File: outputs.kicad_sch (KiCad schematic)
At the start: 2 parts, among them U2 TPS1HB08BQPWPRQ1

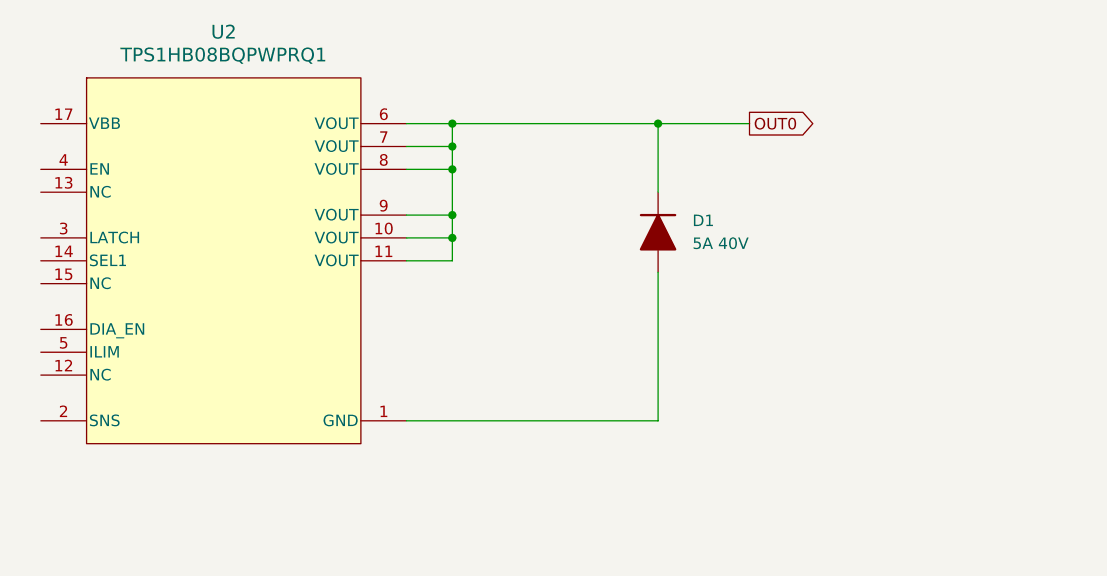
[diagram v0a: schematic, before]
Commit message: More sheets and switching to external FET HSS
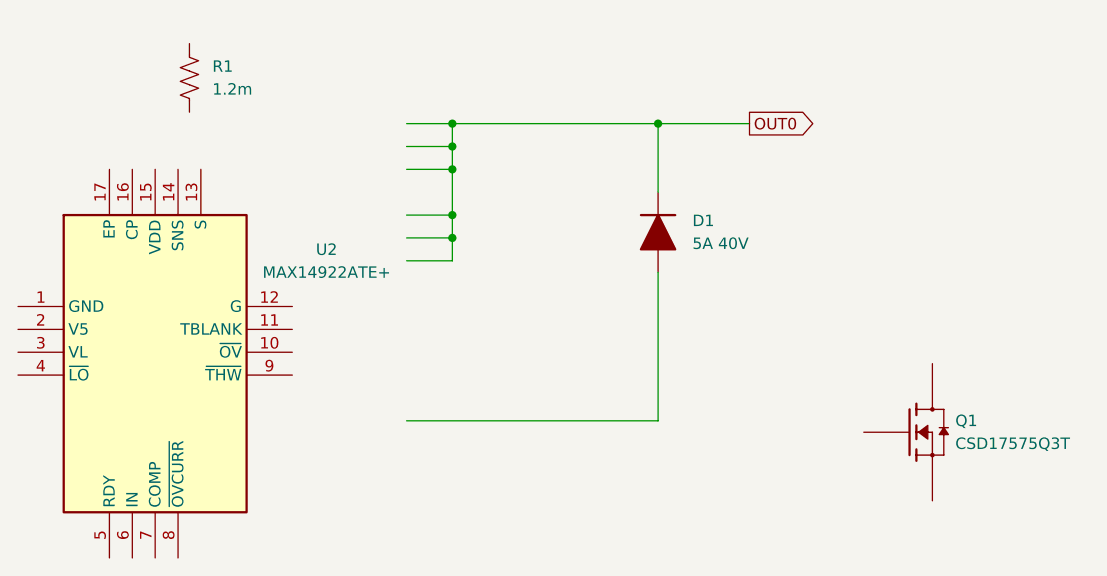
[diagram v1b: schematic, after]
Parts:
- removed U2: TPS1HB08BQPWPRQ1, Sullivan-Labs:PWP0016M-IPC_A, symbol Sullivan-Labs:IC TI High Side Switch 12V 6-70A
- added Q1: CSD17575Q3T, Sullivan-Labs:TRANS_CSD17308Q3, symbol Sullivan-Labs:NMOS 60A 30V
- added R1: 1.2m, Sullivan-Labs:R_2512_6332Metric_Pad1.40x3.35mm_HandSolder, symbol Sullivan-Labs:RES_1.2m_2512
- added U2: MAX14922ATE+, Sullivan-Labs:QFN50P300X300X80-17N, symbol Sullivan-Labs:IC High Side Switch Ex FET
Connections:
- new net: Q1.1 (S), Q1.2 (S), Q1.3 (S)
- new net: Q1.5 (D), Q1.6 (D), Q1.7 (D), Q1.8 (D), Q1.9 (D)
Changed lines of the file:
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@@
+	)
+	(symbol
+		(lib_id "Sullivan-Labs:RES_1.2m_2512")
+		(at 55.88 27.94 0)
+		(unit 1)
+		(exclude_from_sim no)
+		(in_bom yes)
+		(on_board yes)
+		(dnp no)
+		(fields_autoplaced yes)
+		(property "Reference" "R1"
+			(at 58.42 26.6699 0)
+			(effects
+				(font
+					(size 1.27 1.27)
+				)
+				(justify left)
+			)
+		)
+		(property "Value" "1.2m"
+			(at 58.42 29.2099 0)
+			(effects
+				(font
+					(size 1.27 1.27)
+				)
+				(justify left)
+			)
+		)
+		(property "Footprint" "Sullivan-Labs:R_2512_6332Metric_Pad1.40x3.35mm_HandSolder"
+			(at 56.896 28.194 90)
+			(effects
+				(font
+					(size 1.27 1.27)
+				)
+				(hide yes)
+			)
+		)
+		(property "Datasheet" "~"
+			(at 55.88 27.94 0)
+			(effects
+				(font
+					(size 1.27 1.27)
+				)
+				(hide yes)
+			)
+		)
+		(property "Description" "1.2mOhm 5W Shunt Resistor"
+			(at 55.88 27.94 0)
+			(effects
+				(font
+					(size 1.27 1.27)
+				)
+				(hide yes)
+			)
+		)
+		(property "Manufacturer" "VPG Foil Resistors"
+			(at 55.88 27.94 0)
+			(effects
+				(font
+					(size 1.27 1.27)
+				)
+				(hide yes)
+			)
+		)
+		(property "PN" "Y14830R00120F9R"
+			(at 55.88 27.94 0)
+			(effects
+				(font
+					(size 1.27 1.27)
+				)
+				(hide yes)
+			)
+		)
+		(pin "2"
+		)
+		(pin "1"
+		)
+		(instances
+			(project ""
+				(path "/d013d610-c58f-4b11-9d18-37fc135ac516/7b650159-18e3-4a88-b5a2-506e6fe9f3ef"
+					(reference "R1")
+					(unit 1)
+				)
+			)
+		)
+	)
+	(symbol
+		(lib_id "Sullivan-Labs:IC High Side Switch Ex FET")
+		(at 36.83 53.34 0)
+		(unit 1)
+		(exclude_from_sim no)
+		(in_bom yes)
+		(on_board yes)
+		(dnp no)
+		(fields_autoplaced yes)
+		(property "Reference" "U2"
+			(at 71.12 47.0214 0)
+			(effects
+				(font
+					(size 1.27 1.27)
+				)
+			)
+		)
+		(property "Value" "MAX14922ATE+"
+			(at 71.12 49.5614 0)
+			(effects
+				(font
+					(size 1.27 1.27)
+				)
+			)
+		)
+		(property "Footprint" "Sullivan-Labs:QFN50P300X300X80-17N"
+			(at 63.5 140.64 0)
+			(effects
+				(font
+					(size 1.27 1.27)
+				)
+				(justify left top)
+				(hide yes)
+			)
+		)
+		(property "Datasheet" "https://pdfserv.maximintegrated.com/en/ds/MAX14922.pdf"
+			(at 63.5 240.64 0)
+			(effects
+				(font
+					(size 1.27 1.27)
+				)
+				(justify left top)
+				(hide yes)
+			)
+		)
+		(property "Description" "Switching Controllers High-Side Switch Controller"
+			(at 36.83 53.34 0)
+			(effects
+				(font
+					(size 1.27 1.27)
+				)
+				(hide yes)
+			)
+		)
+		(property "Manufacturer" "Analog Devices"
+			(at 63.5 540.64 0)
+			(effects
+				(font
+					(size 1.27 1.27)
+				)
+				(justify left top)
+				(hide yes)
+			)
+		)
+		(property "PN" "MAX14922ATE+"
+			(at 63.5 640.64 0)
+			(effects
+				(font
+					(size 1.27 1.27)
+				)
+				(justify left top)
+				(hide yes)
+			)
+		)
+		(pin "10"
+		)
+		(pin "1"
+		)
+		(pin "17"
+		)
+		(pin "15"
+		)
+		(pin "14"
+		)
+		(pin "13"
+		)
+		(pin "9"
+		)
+		(pin "3"
+		)
+		(pin "2"
+		)
+		(pin "16"
+		)
+		(pin "5"
+		)
+		(pin "11"
+		)
+		(pin "6"
+		)
+		(pin "7"
+		)
+		(pin "8"
+		)
+		(pin "4"
+		)
+		(pin "12"
+		)
+		(instances
+			(project ""
+				(path "/d013d610-c58f-4b11-9d18-37fc135ac516/7b650159-18e3-4a88-b5a2-506e6fe9f3ef"
+					(reference "U2")
+					(unit 1)
+				)
+			)
+		)
 	)
 	(symbol
@@
 	)
 	(symbol
-		(lib_id "Sullivan-Labs:IC TI High Side Switch 12V 6-70A")
-		(at 39.37 33.02 0)
+		(lib_id "Sullivan-Labs:NMOS 60A 30V")
+		(at 135.89 67.31 0)
 		(unit 1)
 		(exclude_from_sim no)
@@
 		(dnp no)
 		(fields_autoplaced yes)
-		(property "Reference" "U2"
-			(at 59.69 22.86 0)
-			(effects
-				(font
-					(size 1.524 1.524)
-				)
-			)
-		)
-		(property "Value" "TPS1HB08BQPWPRQ1"
-			(at 59.69 25.4 0)
-			(effects
-				(font
-					(size 1.524 1.524)
-				)
-			)
-		)
-		(property "Footprint" "Sullivan-Labs:PWP0016M-IPC_A"
-			(at 39.37 33.02 0)
-			(effects
-				(font
-					(size 1.27 1.27)
-					(italic yes)
-				)
-				(hide yes)
-			)
-		)
-		(property "Datasheet" "TPS1HB08BQPWPRQ1"
-			(at 39.37 33.02 0)
-			(effects
-				(font
-					(size 1.27 1.27)
-					(italic yes)
-				)
-				(hide yes)
-			)
-		)
-		(property "Description" "Power Switch ICs - Power Distribution 40-V, 8-mohm, 1-ch automotive smart high-side switch with adjustable current limit 16-HTSSOP -40 to 125"
-			(at 39.37 33.02 0)
-			(effects
-				(font
-					(size 1.27 1.27)
-				)
-				(hide yes)
-			)
-		)
-		(property "Manufacturer" " Texas Instruments"
-			(at 39.37 33.02 0)
-			(effects
-				(font
-					(size 1.27 1.27)
-				)
-				(hide yes)
-			)
-		)
-		(property "PN" "TPS1HB08BQPWPRQ1"
-			(at 39.37 33.02 0)
-			(effects
-				(font
-					(size 1.27 1.27)
-				)
-				(hide yes)
-			)
-		)
-		(pin "10"
+		(property "Reference" "Q1"
+			(at 140.97 66.0399 0)
+			(effects
+				(font
+					(size 1.27 1.27)
+				)
+				(justify left)
+			)
+		)
+		(property "Value" "CSD17575Q3T"
+			(at 140.97 68.5799 0)
+			(effects
+				(font
+					(size 1.27 1.27)
+				)
+				(justify left)
+			)
+		)
+		(property "Footprint" "Sullivan-Labs:TRANS_CSD17308Q3"
+			(at 129.794 92.456 0)
+			(effects
+				(font
+					(size 1.27 1.27)
+				)
+				(justify bottom)
+				(hide yes)
+			)
+		)
+		(property "Datasheet" ""
+			(at 131.318 84.328 0)
+			(effects
+				(font
+					(size 1.27 1.27)
+				)
+				(hide yes)
+			)
+		)
+		(property "Description" "MOSFETs 30V,NCh NexFET Pwr MOSFET"
+			(at 130.556 90.932 0)
+			(effects
+				(font
+					(size 1.27 1.27)
+				)
+				(hide yes)
+			)
+		)
+		(property "Manufacturer" "Texas Instruments"
+			(at 131.318 84.328 0)
+			(effects
+				(font
+					(size 1.27 1.27)
+				)
+				(justify bottom)
+				(hide yes)
+			)
+		)
+		(property "PN" "CSD17575Q3T"
+			(at 131.318 84.328 0)
+			(effects
+				(font
+					(size 1.27 1.27)
+				)
+				(justify bottom)
+				(hide yes)
+			)
+		)
+		(pin "6"
 		)
 		(pin "1"
@@
 		(pin "7"
 		)
+		(pin "9"
+		)
+		(pin "5"
+		)
+		(pin "2"
+		)
+		(pin "4"
+		)
 		(pin "3"
 		)
-		(pin "9"
-		)
-		(pin "17"
-		)
-		(pin "5"
-		)
-		(pin "12"
-		)
-		(pin "2"
-		)
-		(pin "16"
-		)
-		(pin "4"
-		)
-		(pin "15"
-		)
-		(pin "13"
-		)
 		(pin "8"
-		)
-		(pin "6"
-		)
-		(pin "14"
-		)
-		(pin "11"
 		)
 		(instances
 			(project ""
 				(path "/d013d610-c58f-4b11-9d18-37fc135ac516/7b650159-18e3-4a88-b5a2-506e6fe9f3ef"
-					(reference "U2")
+					(reference "Q1")
 					(unit 1)
 				)

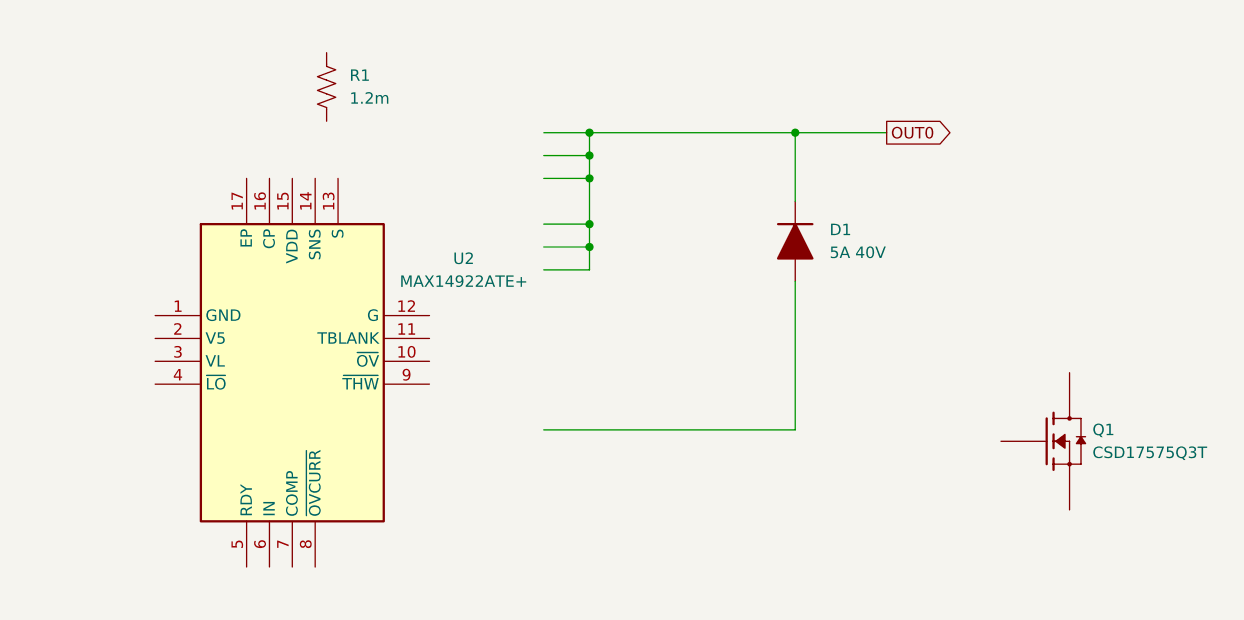
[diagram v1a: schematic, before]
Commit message: Added power domain stuff
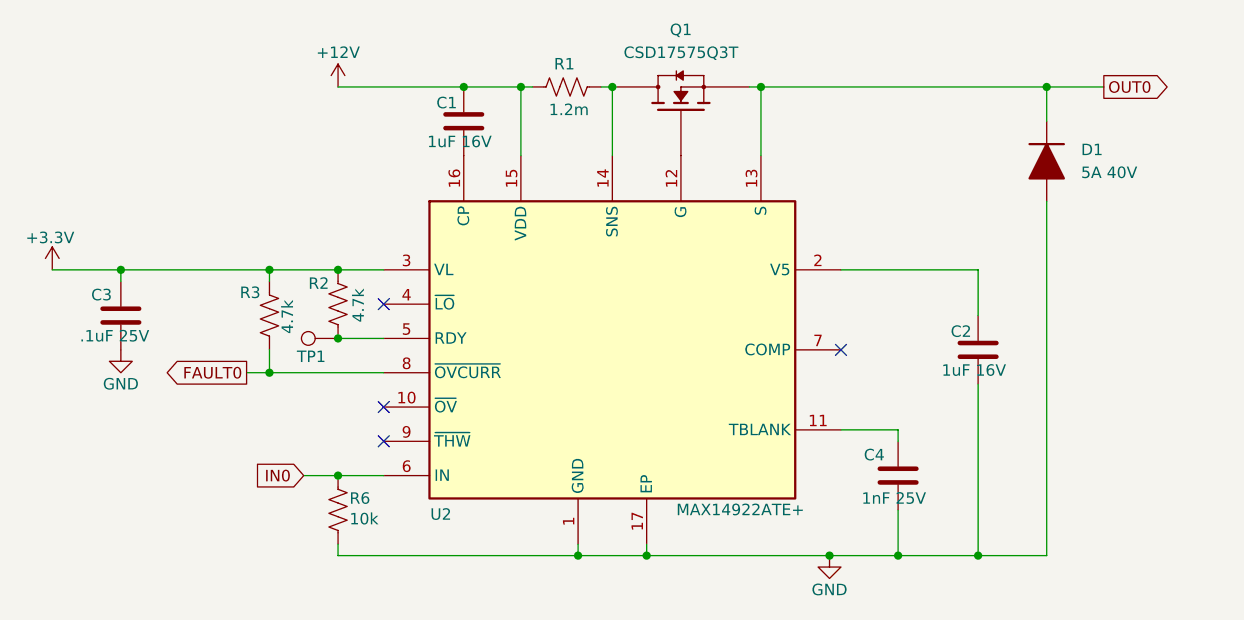
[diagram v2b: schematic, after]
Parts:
- added C1, C2: 1uF 16V, Sullivan-Labs:C_0402_1005Metric, symbol Sullivan-Labs:CAP_1uF_16V_0402
- added C3: .1uF 25V, Sullivan-Labs:C_0402_1005Metric, symbol Sullivan-Labs:CAP_.1uF_25V_0402
- added C4: 1nF 25V, Sullivan-Labs:C_0402_1005Metric, symbol Sullivan-Labs:CAP_1nF_25V_0402
- added R2, R3: 4.7k, Sullivan-Labs:R_0402_1005Metric, symbol Sullivan-Labs:RES_4.7k_0402
- added R6: 10k, Sullivan-Labs:R_0402_1005Metric, symbol Sullivan-Labs:RES_10k_0402
- added TP1: TestPoint, Sullivan-Labs:TestPoint_Pad_D1.0mm, symbol Sullivan-Labs:TP 1mm Circle
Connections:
- net OUT0: now also Q1.1 (S), Q1.2 (S), Q1.3 (S), U2.13 (S)
- net +12V: now reaches R1.1
- net +12V: now also U2.15 (VDD), C1.1
- net at R1.2: now also Q1.5 (D), Q1.6 (D), Q1.7 (D), Q1.8 (D), Q1.9 (D), U2.14 (SNS)
- net GND: now reaches U2.1 (GND)
- net GND: now also D1.2 (A), U2.17 (EP), C2.2, C3.2, C4.2, R6.2
- net at U2.11 (TBLANK): now also C4.1
- net at U2.12 (G): now also Q1.4 (G)
- net at U2.16 (CP): now also C1.2
- net at U2.2 (V5): now also C2.1
- net +3.3V: now reaches U2.3 (VL)
- net +3.3V: now also C3.1, R2.1, R3.1
- net at U2.5 (RDY): now also R2.2, TP1.1
- net IN0: now reaches U2.6 (IN)
- net IN0: now also R6.1
- net FAULT0: now reaches U2.8 (~{OVCURR})
- net FAULT0: now also R3.2
- no-connect marks 0 -> 4
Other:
- moved on the sheet: D1, Q1, R1, U2

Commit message: Small changes to schematic
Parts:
- added R43: 4.7k, Sullivan-Labs:R_0402_1005Metric, symbol Sullivan-Labs:RES_4.7k_0402
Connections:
- net +3.3V: now also R43.1
- net OVERHEAT: now reaches U2.9 (~{THW})
- net OVERHEAT: now also R43.2
- no-connect marks 4 -> 3
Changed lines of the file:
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@@
-	)
-	(no_connect
-		(at 62.23 67.31)
 	)
 	(no_connect
@@
 	(wire
 		(pts
+			(xy 46.99 67.31) (xy 62.23 67.31)
+		)
+		(stroke
+			(width 0)
+			(type default)
+		)
+	)
+	(wire
+		(pts
 			(xy 135.89 27.94) (xy 135.89 31.75)
 		)
@@
 	(wire
 		(pts
+			(xy 243.84 120.65) (xy 246.38 120.65)
+		)
+		(stroke
+			(width 0)
+			(type default)
+		)
+	)
+	(wire
+		(pts
 			(xy 77.47 27.94) (xy 78.74 27.94)
 		)
@@
 		(pts
 			(xy 49.53 49.53) (xy 49.53 48.26)
+		)
+		(stroke
+			(width 0)
+			(type default)
+		)
+	)
+	(wire
+		(pts
+			(xy 246.38 119.38) (xy 246.38 120.65)
 		)
 		(stroke
@@
 		(property "Intersheetrefs" "${INTERSHEET_REFS}"
 			(at 47.21 71.12 0)
+			(effects
+				(font
+					(size 1.27 1.27)
+				)
+				(justify right)
+				(hide yes)
+			)
+		)
+	)
+	(global_label "OVERHEAT"
+		(shape output)
+		(at 46.99 67.31 180)
+		(fields_autoplaced yes)
+		(effects
+			(font
+				(size 1.27 1.27)
+			)
+			(justify right)
+		)
+		(property "Intersheetrefs" "${INTERSHEET_REFS}"
+			(at 34.631 67.31 0)
+			(effects
+				(font
+					(size 1.27 1.27)
+				)
+				(justify right)
+				(hide yes)
+			)
+		)
+	)
+	(global_label "OVERHEAT"
+		(shape output)
+		(at 243.84 120.65 180)
+		(fields_autoplaced yes)
+		(effects
+			(font
+				(size 1.27 1.27)
+			)
+			(justify right)
+		)
+		(property "Intersheetrefs" "${INTERSHEET_REFS}"
+			(at 231.481 120.65 0)
 			(effects
 				(font
@@
 	)
 	(symbol
+		(lib_id "Sullivan-Labs:RES_4.7k_0402")
+		(at 246.38 115.57 0)
+		(unit 1)
+		(exclude_from_sim no)
+		(in_bom yes)
+		(on_board yes)
+		(dnp no)
+		(property "Reference" "R43"
+			(at 244.094 117.348 90)
+			(effects
+				(font
+					(size 1.27 1.27)
+				)
+				(justify left)
+			)
+		)
+		(property "Value" "4.7k"
+			(at 248.412 117.602 90)
+			(effects
+				(font
+					(size 1.27 1.27)
+				)
+				(justify left)
+			)
+		)
+		(property "Footprint" "Sullivan-Labs:R_0402_1005Metric"
+			(at 247.396 115.824 90)
+			(effects
+				(font
+					(size 1.27 1.27)
+				)
+				(hide yes)
+			)
+		)
+		(property "Datasheet" "~"
+			(at 246.38 115.57 0)
+			(effects
+				(font
+					(size 1.27 1.27)
+				)
+				(hide yes)
+			)
+		)
+		(property "Description" "4.7kOhm 1% 0402 Resistor"
+			(at 246.38 115.57 0)
+			(effects
+				(font
+					(size 1.27 1.27)
+				)
+				(hide yes)
+			)
+		)
+		(property "Manufacturer" "Yageo"
+			(at 246.38 115.57 0)
+			(effects
+				(font
+					(size 1.27 1.27)
+				)
+				(hide yes)
+			)
+		)
+		(property "PN" "RC0402FR-074K7L"
+			(at 246.38 115.57 0)
+			(effects
+				(font
+					(size 1.27 1.27)
+				)
+				(hide yes)
+			)
+		)
+		(pin "1"
+		)
+		(pin "2"
+		)
+		(instances
+			(project "cooler-master"
+				(path "/d013d610-c58f-4b11-9d18-37fc135ac516/7b650159-18e3-4a88-b5a2-506e6fe9f3ef"
+					(reference "R43")
+					(unit 1)
+				)
+			)
+		)
+	)
+	(symbol
 		(lib_id "Sullivan-Labs:CAP_1uF_16V_0402")
 		(at 71.12 31.75 0)
@@
 					(unit 1)
 				)
+			)
+		)
+	)
+	(symbol
+		(lib_id "power:+3.3V")
+		(at 246.38 111.76 0)
+		(unit 1)
+		(exclude_from_sim no)
+		(in_bom yes)
+		(on_board yes)
+		(dnp no)
+		(property "Reference" "#PWR055"
+			(at 246.38 115.57 0)
+			(effects
+				(font
+					(size 1.27 1.27)
+				)
+				(hide yes)
+			)
+		)
+		(property "Value" "+3.3V"
+			(at 246.126 108.204 0)
+			(effects
+				(font
+					(size 1.27 1.27)
+				)
+			)
+		)
+		(property "Footprint" ""
+			(at 246.38 111.76 0)
+			(effects
+				(font
+					(size 1.27 1.27)
+				)
+				(hide yes)
+			)
+		)
+		(property "Datasheet" ""
+			(at 246.38 111.76 0)
+			(effects
+				(font
+					(size 1.27 1.27)
+				)
+				(hide yes)
+			)
+		)
+		(property "Description" "Power symbol creates a global label with name \"+3.3V\""
+			(at 246.38 111.76 0)
+			(effects
+				(font
+					(size 1.27 1.27)
+				)
+				(hide yes)
+			)
+		)
+		(pin "1"
+		)
+		(instances
+			(project "cooler-master"
+				(path "/d013d610-c58f-4b11-9d18-37fc135ac516/7b650159-18e3-4a88-b5a2-506e6fe9f3ef"
+					(reference "#PWR055")
+					(unit 1)
+				)

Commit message: Initial schematic is done
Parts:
- added C40, C44, C48: .1uF 25V, Sullivan-Labs:C_0402_1005Metric, symbol Sullivan-Labs:CAP_.1uF_25V_0402
- added C41, C43, C45, C47, C49, C51: 1uF 16V, Sullivan-Labs:C_0402_1005Metric, symbol Sullivan-Labs:CAP_1uF_16V_0402
- added C42, C46, C50: 1nF 25V, Sullivan-Labs:C_0402_1005Metric, symbol Sullivan-Labs:CAP_1nF_25V_0402
- added D10, D11, D12: 5A 40V, Sullivan-Labs:DO-214AC, symbol Sullivan-Labs:DIODE 5A 40V Schottkey
- added F1, F2: 1.5A, Sullivan-Labs:FUSC1608X56N, symbol Sullivan-Labs:FUSE 1.5A Fast Blow
- added Q10, Q9: SSM3K339R_LF, Sullivan-Labs:SOT-23F_TOS, symbol Sullivan-Labs:NMOS 40V 2A
- added Q6, Q7, Q8: CSD17575Q3T, Sullivan-Labs:TRANS_CSD17308Q3, symbol Sullivan-Labs:NMOS 60A 30V
- added R53, R54, R57, R58, R61, R62: 4.7k, Sullivan-Labs:R_0402_1005Metric, symbol Sullivan-Labs:RES_4.7k_0402
- added R55, R59, R63, R65, R66: 10k, Sullivan-Labs:R_0402_1005Metric, symbol Sullivan-Labs:RES_10k_0402
- added R56, R60, R64: 1.2m, Sullivan-Labs:R_2512_6332Metric_Pad1.40x3.35mm_HandSolder, symbol Sullivan-Labs:RES_1.2m_2512
- added R67, R68: 100R, Sullivan-Labs:R_0402_1005Metric, symbol Sullivan-Labs:RES_100R_0402
- added TP4, TP5, TP6: TestPoint, Sullivan-Labs:TestPoint_Pad_D1.0mm, symbol Sullivan-Labs:TP 1mm Circle
- added U10, U11, U12: MAX14922ATE+, Sullivan-Labs:QFN50P300X300X80-17N, symbol Sullivan-Labs:IC High Side Switch Ex FET
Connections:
- net +12V: now also C41.1, C45.1, C49.1, R56.1, R60.1, R64.1, U10.15 (VDD), U11.15 (VDD), U12.15 (VDD)
- net +3.3V: now also C40.1, C44.1, C48.1, R53.1, R54.1, R57.1, R58.1, R61.1, R62.1, U10.3 (VL), U11.3 (VL), U12.3 (VL)
- net GND: now also C40.2, C42.2, C43.2, C44.2, C46.2, C47.2, C48.2, C50.2, C51.2, D10.2 (A), D11.2 (A), D12.2 (A), Q10.2, Q9.2, R55.2, R59.2, R63.2, R65.2, R66.2, U10.1 (GND), U10.17 (EP), U11.1 (GND), U11.17 (EP), U12.1 (GND), U12.17 (EP)
- net OVERHEAT: now also U10.9 (~{THW}), U11.9 (~{THW}), U12.9 (~{THW})
- net IN0 renamed EN0
- new net: C51.1, U12.2 (V5)
- new net: C46.1, U11.11 (TBLANK)
- new net: Q8.4 (G), U12.12 (G)
- new net: Q8.5 (D), Q8.6 (D), Q8.7 (D), Q8.8 (D), Q8.9 (D), R64.2, U12.14 (SNS)
- new net: C50.1, U12.11 (TBLANK)
- new net: C49.2, U12.16 (CP)
- new net: R62.2, TP6.1, U12.5 (RDY)
- new net: F2.1, Q10.3
- new net: Q10.1, R66.1, R68.2
- new net: Q6.4 (G), U10.12 (G)
- new net: Q6.5 (D), Q6.6 (D), Q6.7 (D), Q6.8 (D), Q6.9 (D), R56.2, U10.14 (SNS)
- new net: R58.2, TP5.1, U11.5 (RDY)
- new net: R54.2, TP4.1, U10.5 (RDY)
- new net: C47.1, U11.2 (V5)
- new net: C43.1, U10.2 (V5)
- new net: C42.1, U10.11 (TBLANK)
- new net: Q7.4 (G), U11.12 (G)
- new net: Q7.5 (D), Q7.6 (D), Q7.7 (D), Q7.8 (D), Q7.9 (D), R60.2, U11.14 (SNS)
- new net: Q9.1, R65.1, R67.2
- new net: C41.2, U10.16 (CP)
- new net: C45.2, U11.16 (CP)
- new net: F1.1, Q9.3
- new net EN1: R55.1, U10.6 (IN)
- new net EN2: R59.1, U11.6 (IN)
- new net EN3: R63.1, U12.6 (IN)
- new net FAULT1: R53.2, U10.8 (~{OVCURR})
- new net FAULT2: R57.2, U11.8 (~{OVCURR})
- new net FAULT3: R61.2, U12.8 (~{OVCURR})
- new net LP_EN0: R67.1, R68.1
- new net LP_OUT0: F1.2
- new net LP_OUT1: F2.2
- new net OUT1: D10.1 (K), Q6.1 (S), Q6.2 (S), Q6.3 (S), U10.13 (S)
- new net OUT2: D11.1 (K), Q7.1 (S), Q7.2 (S), Q7.3 (S), U11.13 (S)
- new net OUT3: D12.1 (K), Q8.1 (S), Q8.2 (S), Q8.3 (S), U12.13 (S)
- no-connect marks 3 -> 12
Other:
- moved on the sheet: C1, C2, C3, C4, D1, R1, R2, R3, R43, R6, TP1, U2
